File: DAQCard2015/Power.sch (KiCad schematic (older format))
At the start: 0 parts

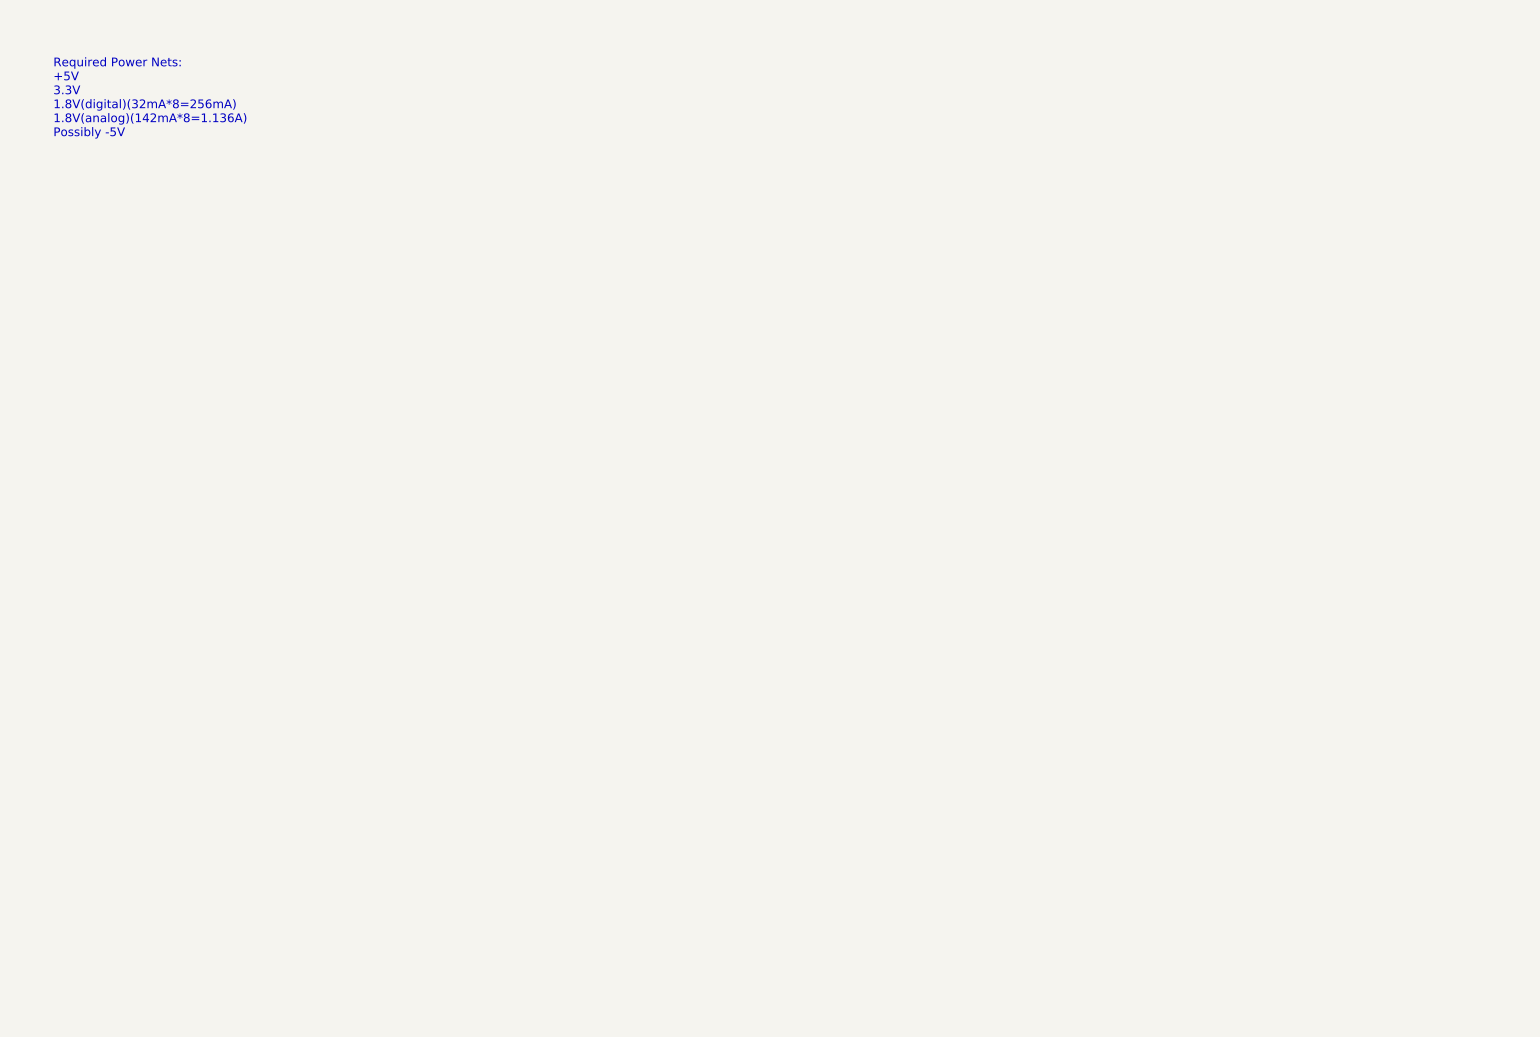
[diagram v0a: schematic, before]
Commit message: Adds power circuitry to DAQCard2015
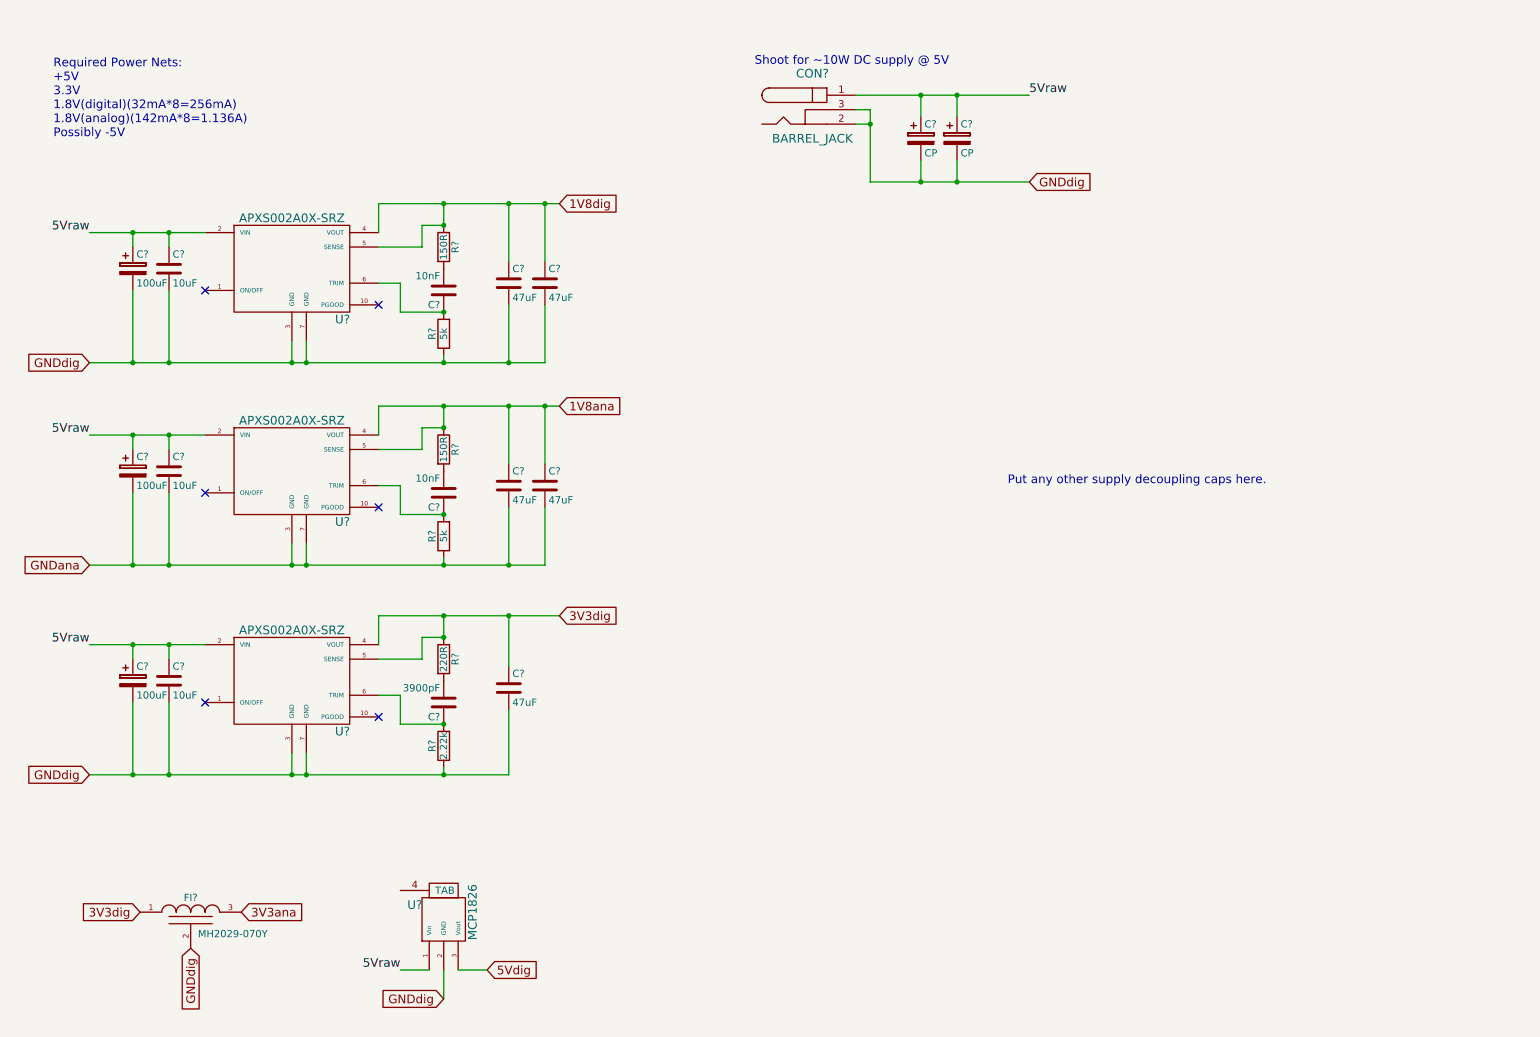
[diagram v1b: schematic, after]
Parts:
- added C? (x3): 100uF, symbol CP
- added C? (x3): 10uF, symbol C
- added C? (x2): 10nF, symbol C
- added C? (x5): 47uF, symbol C
- added C?: 3900pF, symbol C
- added C? (x2): CP, symbol CP
- added CON?: BARREL_JACK, symbol BARREL_JACK
- added FI?: MH2029-070Y, symbol EMI_FILTER2
- added R? (x2): 150R, symbol R
- added R? (x2): 5k, symbol R
- added R?: 220R, symbol R
- added R?: 2.22k, symbol R
- added U? (x3): APXS002A0X-SRZ, symbol APXS002A0X-SRZ
- added U?: MCP1826, symbol MCP1826
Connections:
- new net: C?.1, R?.2, U?.6 (TRIM) (x3)
- new net: C?.2, R?.2 (x3)
- new net 1V8ana: C?.1, C?.1, R?.1, U?.4 (VOUT), U?.5 (SENSE)
- new net 1V8dig: C?.1, C?.1, R?.1, U?.4 (VOUT), U?.5 (SENSE)
- new net 3V3ana: FI?.3 (VO)
- new net 3V3dig: C?.1, FI?.1 (VI), R?.1, U?.4 (VOUT), U?.5 (SENSE)
- new net 5Vdig: U?.3 (Vout)
- new net 5Vraw: C?.1, C?.1, C?.1, C?.1, C?.1, C?.1, C?.1, C?.1, CON?.1, U?.1 (Vin), U?.2 (VIN), U?.2 (VIN), U?.2 (VIN)
- new net GNDana: C?.2, C?.2, C?.2, C?.2, R?.1, U?.3 (GND), U?.7 (GND)
- new net GNDdig: C?.2, C?.2, C?.2, C?.2, C?.2, C?.2, C?.2, C?.2, C?.2, CON?.2, CON?.3, FI?.2 (GND), R?.1, R?.1, U?.2 (GND), U?.3 (GND), U?.3 (GND), U?.7 (GND), U?.7 (GND)
- no-connect marks 0 -> 6
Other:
- note added: "Put any other supply decoupling caps here."
- note added: "Shoot for ~~10W DC supply @ 5V"

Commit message: Replaces single ample with 4-channel varients. Greatly reducing part count
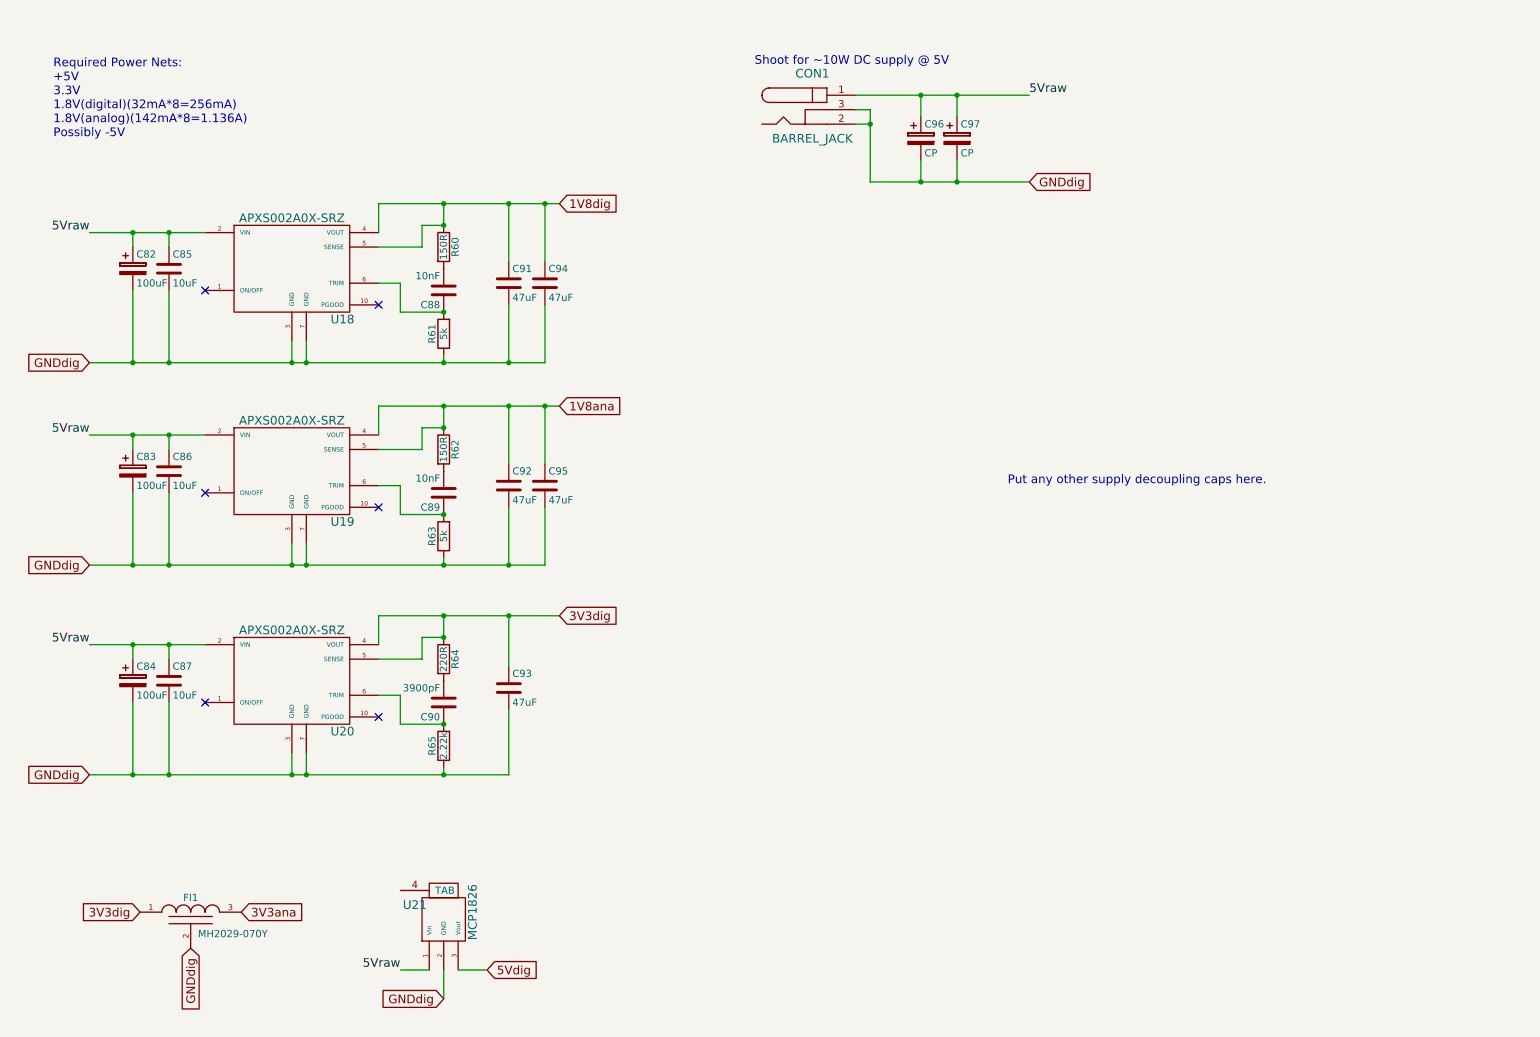
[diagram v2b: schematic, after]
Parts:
- gave numbers to parts that had none: 28
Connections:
- net GNDana is gone; now on net GNDdig: C83.2, C86.2, C92.2, C95.2, R63.1, U19.3 (GND), U19.7 (GND)
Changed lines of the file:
@@
 Required Power Nets:\n+5V\n3.3V\n1.8V(digital)(32mA*8=256mA)\n1.8V(analog)(142mA*8=1.136A)\nPossibly -5V
 $Comp
-L APXS002A0X-SRZ U?
+L APXS002A0X-SRZ U18
 U 1 1 55CC1B62
 P 2600 2050
-F 0 "U?" H 2950 1700 60  0000 C CNN
+F 0 "U18" H 2950 1700 60  0000 C CNN
 F 1 "APXS002A0X-SRZ" H 2600 2400 60  0000 C CNN
 F 2 "" H 2250 1400 60  0000 C CNN
@@
 $EndComp
 $Comp
-L CP C?
+L CP C82
 U 1 1 55CC28F2
 P 1500 2050
-F 0 "C?" H 1525 2150 50  0000 L CNN
+F 0 "C82" H 1525 2150 50  0000 L CNN
 F 1 "100uF" H 1525 1950 50  0000 L CNN
 F 2 "" H 1538 1900 30  0000 C CNN
@@
 $EndComp
 $Comp
-L C C?
+L C C85
 U 1 1 55CC2951
 P 1750 2050
-F 0 "C?" H 1775 2150 50  0000 L CNN
+F 0 "C85" H 1775 2150 50  0000 L CNN
 F 1 "10uF" H 1775 1950 50  0000 L CNN
 F 2 "" H 1788 1900 30  0000 C CNN
@@
 $EndComp
 $Comp
-L R R?
+L R R60
 U 1 1 55CC29C3
 P 3650 1900
-F 0 "R?" V 3730 1900 50  0000 C CNN
+F 0 "R60" V 3730 1900 50  0000 C CNN
 F 1 "150R" V 3650 1900 50  0000 C CNN
 F 2 "" V 3580 1900 30  0000 C CNN
@@
 $EndComp
 $Comp
-L R R?
+L R R61
 U 1 1 55CC2A10
 P 3650 2500
-F 0 "R?" V 3730 2500 50  0000 C CNN
+F 0 "R61" V 3730 2500 50  0000 C CNN
 F 1 "5k" V 3650 2500 50  0000 C CNN
 F 2 "" V 3580 2500 30  0000 C CNN
@@
 $EndComp
 $Comp
-L C C?
+L C C88
 U 1 1 55CC2A89
 P 3650 2200
-F 0 "C?" H 3675 2300 50  0000 L CNN
+F 0 "C88" H 3675 2300 50  0000 L CNN
 F 1 "10nF" H 3675 2100 50  0000 L CNN
 F 2 "" H 3688 2050 30  0000 C CNN
@@
 $EndComp
 $Comp
-L C C?
+L C C91
 U 1 1 55CC2AEA
 P 4100 2150
-F 0 "C?" H 4125 2250 50  0000 L CNN
+F 0 "C91" H 4125 2250 50  0000 L CNN
 F 1 "47uF" H 4125 2050 50  0000 L CNN
 F 2 "" H 4138 2000 30  0000 C CNN
@@
 Connection ~ 1500 2700
 $Comp
-L C C?
+L C C94
 U 1 1 55CC4361
 P 4350 2150
-F 0 "C?" H 4375 2250 50  0000 L CNN
+F 0 "C94" H 4375 2250 50  0000 L CNN
 F 1 "47uF" H 4375 2050 50  0000 L CNN
 F 2 "" H 4388 2000 30  0000 C CNN
@@
 GNDdig
 $Comp
-L APXS002A0X-SRZ U?
+L APXS002A0X-SRZ U19
 U 1 1 55CC74F0
 P 2600 3450
-F 0 "U?" H 2950 3100 60  0000 C CNN
+F 0 "U19" H 2950 3100 60  0000 C CNN
 F 1 "APXS002A0X-SRZ" H 2600 3800 60  0000 C CNN
 F 2 "" H 2250 2800 60  0000 C CNN
@@
 $EndComp
 $Comp
-L CP C?
+L CP C83
 U 1 1 55CC74F7
 P 1500 3450
-F 0 "C?" H 1525 3550 50  0000 L CNN
+F 0 "C83" H 1525 3550 50  0000 L CNN
 F 1 "100uF" H 1525 3350 50  0000 L CNN
 F 2 "" H 1538 3300 30  0000 C CNN
@@
 $EndComp
 $Comp
-L C C?
+L C C86
 U 1 1 55CC74FD
 P 1750 3450
-F 0 "C?" H 1775 3550 50  0000 L CNN
+F 0 "C86" H 1775 3550 50  0000 L CNN
 F 1 "10uF" H 1775 3350 50  0000 L CNN
 F 2 "" H 1788 3300 30  0000 C CNN
@@
 $EndComp
 $Comp
-L R R?
+L R R62
 U 1 1 55CC7503
 P 3650 3300
-F 0 "R?" V 3730 3300 50  0000 C CNN
+F 0 "R62" V 3730 3300 50  0000 C CNN
 F 1 "150R" V 3650 3300 50  0000 C CNN
 F 2 "" V 3580 3300 30  0000 C CNN
@@
 $EndComp
 $Comp
-L R R?
+L R R63
 U 1 1 55CC7509
 P 3650 3900
-F 0 "R?" V 3730 3900 50  0000 C CNN
+F 0 "R63" V 3730 3900 50  0000 C CNN
 F 1 "5k" V 3650 3900 50  0000 C CNN
 F 2 "" V 3580 3900 30  0000 C CNN
@@
 $EndComp
 $Comp
-L C C?
+L C C89
 U 1 1 55CC750F
 P 3650 3600
-F 0 "C?" H 3675 3700 50  0000 L CNN
+F 0 "C89" H 3675 3700 50  0000 L CNN
 F 1 "10nF" H 3675 3500 50  0000 L CNN
 F 2 "" H 3688 3450 30  0000 C CNN
@@
 $EndComp
 $Comp
-L C C?
+L C C92
 U 1 1 55CC7515
 P 4100 3550
-F 0 "C?" H 4125 3650 50  0000 L CNN
+F 0 "C92" H 4125 3650 50  0000 L CNN
 F 1 "47uF" H 4125 3450 50  0000 L CNN
 F 2 "" H 4138 3400 30  0000 C CNN
@@
 Connection ~ 1500 4100
 $Comp
-L C C?
+L C C95
 U 1 1 55CC7546
 P 4350 3550
-F 0 "C?" H 4375 3650 50  0000 L CNN
+F 0 "C95" H 4375 3650 50  0000 L CNN
 F 1 "47uF" H 4375 3450 50  0000 L CNN
 F 2 "" H 4388 3400 30  0000 C CNN
@@
 1V8ana
 Text GLabel 1200 4100 0    60   Input ~ 0
-GNDana
-$Comp
-L APXS002A0X-SRZ U?
+GNDdig
+$Comp
+L APXS002A0X-SRZ U20
 U 1 1 55CC7C26
 P 2600 4900
-F 0 "U?" H 2950 4550 60  0000 C CNN
+F 0 "U20" H 2950 4550 60  0000 C CNN
 F 1 "APXS002A0X-SRZ" H 2600 5250 60  0000 C CNN
 F 2 "" H 2250 4250 60  0000 C CNN
@@
 $EndComp
 $Comp
-L CP C?
+L CP C84
 U 1 1 55CC7C2D
 P 1500 4900
-F 0 "C?" H 1525 5000 50  0000 L CNN
+F 0 "C84" H 1525 5000 50  0000 L CNN
 F 1 "100uF" H 1525 4800 50  0000 L CNN
 F 2 "" H 1538 4750 30  0000 C CNN
@@
 $EndComp
 $Comp
-L C C?
+L C C87
 U 1 1 55CC7C33
 P 1750 4900
-F 0 "C?" H 1775 5000 50  0000 L CNN
+F 0 "C87" H 1775 5000 50  0000 L CNN
 F 1 "10uF" H 1775 4800 50  0000 L CNN
 F 2 "" H 1788 4750 30  0000 C CNN
@@
 $EndComp
 $Comp
-L R R?
+L R R64
 U 1 1 55CC7C39
 P 3650 4750
-F 0 "R?" V 3730 4750 50  0000 C CNN
+F 0 "R64" V 3730 4750 50  0000 C CNN
 F 1 "220R" V 3650 4750 50  0000 C CNN
 F 2 "" V 3580 4750 30  0000 C CNN
@@
 $EndComp
 $Comp
-L R R?
+L R R65
 U 1 1 55CC7C3F
 P 3650 5350
-F 0 "R?" V 3730 5350 50  0000 C CNN
+F 0 "R65" V 3730 5350 50  0000 C CNN
 F 1 "2.22k" V 3650 5350 50  0000 C CNN
 F 2 "" V 3580 5350 30  0000 C CNN
@@
 $EndComp
 $Comp
-L C C?
+L C C90
 U 1 1 55CC7C45
 P 3650 5050
-F 0 "C?" H 3675 5150 50  0000 L CNN
+F 0 "C90" H 3675 5150 50  0000 L CNN
 F 1 "3900pF" H 3675 4950 50  0000 L CNN
 F 2 "" H 3688 4900 30  0000 C CNN
@@
 $EndComp
 $Comp
-L C C?
+L C C93
 U 1 1 55CC7C4B
 P 4100 4950
-F 0 "C?" H 4125 5050 50  0000 L CNN
+F 0 "C93" H 4125 5050 50  0000 L CNN
 F 1 "47uF" H 4125 4850 50  0000 L CNN
 F 2 "" H 4138 4800 30  0000 C CNN
@@
 GNDdig
 $Comp
-L EMI_FILTER2 FI?
+L EMI_FILTER2 FI1
 U 1 1 55CCBDB6
 P 1900 6500
-F 0 "FI?" H 1900 6600 50  0000 C CNN
+F 0 "FI1" H 1900 6600 50  0000 C CNN
 F 1 "MH2029-070Y" H 1950 6350 50  0000 L CNN
 F 2 "" H 1900 6500 60  0000 C CNN
@@
 GNDdig
 $Comp
-L MCP1826 U?
+L MCP1826 U21
 U 1 1 55CCD241
 P 3650 6700
-F 0 "U?" H 3450 6950 60  0000 C CNN
+F 0 "U21" H 3450 6950 60  0000 C CNN
 F 1 "MCP1826" V 3850 6900 60  0000 C CNN
 F 2 "" H 3650 6700 60  0000 C CNN
@@
 GNDdig
 $Comp
-L BARREL_JACK CON?
+L BARREL_JACK CON1
 U 1 1 55CCF566
 P 6200 950
-F 0 "CON?" H 6200 1200 60  0000 C CNN
+F 0 "CON1" H 6200 1200 60  0000 C CNN
 F 1 "BARREL_JACK" H 6200 750 60  0000 C CNN
 F 2 "" H 6200 950 60  0000 C CNN
@@
 	6600 1450 7700 1450
 $Comp
-L CP C?
+L CP C96
 U 1 1 55CD0228
 P 6950 1150
-F 0 "C?" H 6975 1250 50  0000 L CNN
+F 0 "C96" H 6975 1250 50  0000 L CNN
 F 1 "CP" H 6975 1050 50  0000 L CNN
 F 2 "" H 6988 1000 30  0000 C CNN
@@
 $EndComp
 $Comp
-L CP C?
+L CP C97
 U 1 1 55CD029E
 P 7200 1150
-F 0 "C?" H 7225 1250 50  0000 L CNN
+F 0 "C97" H 7225 1250 50  0000 L CNN
 F 1 "CP" H 7225 1050 50  0000 L CNN
 F 2 "" H 7238 1000 30  0000 C CNN
